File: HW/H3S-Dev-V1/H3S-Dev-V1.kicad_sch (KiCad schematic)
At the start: 50 parts, among them J1 USB_C_Receptacle_USB2.0_16P, J2 Conn_01x02, J3 Conn_Coaxial, J4 Conn_01x04, J5 Conn_01x04, Q1 DMP3099L, SW1 SW_Push, U1 Ra-01SH-P, U2 LTC4054ES5-4.2, U3 USBLC6-2SC6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

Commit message: Minor changes
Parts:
- C10, C11: footprint Capacitor_SMD:C_0603_1608Metric -> Capacitor_SMD:C_0402_1005Metric
- R18: footprint Resistor_SMD:R_0603_1608Metric -> Resistor_SMD:R_0402_1005Metric
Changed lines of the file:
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@@
 			)
 		)
-		(property "Footprint" "Resistor_SMD:R_0603_1608Metric"
+		(property "Footprint" "Resistor_SMD:R_0402_1005Metric"
 			(at 266.7 66.548 90)
 			(effects
@@
 			)
 		)
-		(property "Footprint" "Capacitor_SMD:C_0603_1608Metric"
+		(property "Footprint" "Capacitor_SMD:C_0402_1005Metric"
 			(at 272.7452 74.93 0)
 			(effects
@@
 			)
 		)
-		(property "Footprint" "Capacitor_SMD:C_0603_1608Metric"
+		(property "Footprint" "Capacitor_SMD:C_0402_1005Metric"
 			(at 262.5852 74.93 0)
 			(effects

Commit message: Some progress
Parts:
- added C12: 1u, Capacitor_SMD:C_0603_1608Metric, symbol Device:C
- added C13: 100n, Capacitor_SMD:C_0603_1608Metric, symbol Device:C
- added D2, D4: LED, LED_SMD:LED_0603_1608Metric, symbol Device:LED
- added R20, R21, R22: 10k, Resistor_SMD:R_0603_1608Metric, symbol Device:R
- added R23, R24, R25, R26, R27: 20, Resistor_SMD:R_0603_1608Metric, symbol Device:R
- added R28, R29: 0, Resistor_SMD:R_0603_1608Metric, symbol Device:R
- added SW2: SW_Push, Button_Switch_SMD:SW_Tactile_SPST_NO_Straight_CK_PTS636Sx25SMTRLFS, symbol Switch:SW_Push
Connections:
- net GND: now also C12.2, C13.2, R21.2, R22.2, SW2.2
- net SCL: now also R28.1
- net SDA: now also R29.1
- net VCC: now also D2.2 (A), R20.1
- net G_3D: now reaches U6.2 (3D_FIX)
- net G_JD: now reaches U6.20 (JAM_DET)
- net ~{G_RESET}: now reaches U6.23 (~{RESET})
- net ~{G_RESET}: now also R25.2
- net G_GF: now reaches U6.24 (GEO_FENCE)
- net G_TX: now reaches U6.25 (TXD1)
- net G_TX: now also R24.2
- net G_RX: now reaches U6.26 (RXD1)
- net G_RX: now also R23.2
- net G_FO: now reaches U6.28 (FORCE_ON)
- net G_FO: now also R27.2
- net G_TP: now reaches U6.29 (TIMEPULSE)
- net G_TP: now also D4.2 (A)
- net G_SDA: now reaches U6.3 (I2C_SDA)
- net G_SDA: now also R29.2
- net G_SCL: now reaches U6.6 (I2C_SCL)
- net G_SCL: now also R28.2
- net G_INT: now reaches U6.7 (EXTINT0)
- net G_INT: now also R26.2
- net ~{ESP_IO0}: now reaches U4.27 (IO0)
- net ~{ESP_IO0}: now also C12.1, C13.1, R20.2, SW2.1
- new net: D2.1 (K), R21.1
- new net: D4.1 (K), R22.1
- new net FO: R27.1
- new net INT: R26.1
- new net RX: R23.1
- new net TX: R24.1
- new net ~{G_RST}: R25.1
- no-connect marks 8 -> 7
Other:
- note added: "BOOT"
- note added: "RESET"
- moved on the sheet: C1, C10, C11, C2, C3, C4, C5, C6, C7, C8, C9, D1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

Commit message: Some progress
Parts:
- added R30, R31, R32, R33: 0, Resistor_SMD:R_0603_1608Metric, symbol Device:R
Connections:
- net G_3D: now also R31.1
- net G_GF: now also R32.1
- net G_JD: now also R33.1
- net G_TP: now also R30.1
- new net 3D: R31.2
- new net GF: R32.2
- new net JD: R33.2
- new net TP: R30.2
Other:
- moved on the sheet: C1, C10, C11, C12, C13, C2, C3, C4, C5, C6, C7, C8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

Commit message: Some progress
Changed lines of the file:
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@@
 	(wire
 		(pts
-			(xy 92.71 134.62) (xy 92.71 151.13)
+			(xy 92.71 134.62) (xy 92.71 152.4)
 		)
 		(stroke
@@
 	(symbol
 		(lib_id "power:GND")
-		(at 92.71 151.13 0)
+		(at 92.71 152.4 0)
 		(unit 1)
 		(exclude_from_sim no)
@@
 		(fields_autoplaced yes)
 		(property "Reference" "#PWR017"
-			(at 92.71 157.48 0)
+			(at 92.71 158.75 0)
 			(effects
 				(font
@@
 		)
 		(property "Value" "GND"
-			(at 92.71 156.21 0)
+			(at 92.71 157.48 0)
 			(effects
 				(font
@@
 		)
 		(property "Footprint" ""
-			(at 92.71 151.13 0)
+			(at 92.71 152.4 0)
 			(effects
 				(font
@@
 		)
 		(property "Datasheet" ""
-			(at 92.71 151.13 0)
+			(at 92.71 152.4 0)
 			(effects
 				(font
@@
 		)
 		(property "Description" "Power symbol creates a global label with name \"GND\" , ground"
-			(at 92.71 151.13 0)
+			(at 92.71 152.4 0)
 			(effects
 				(font

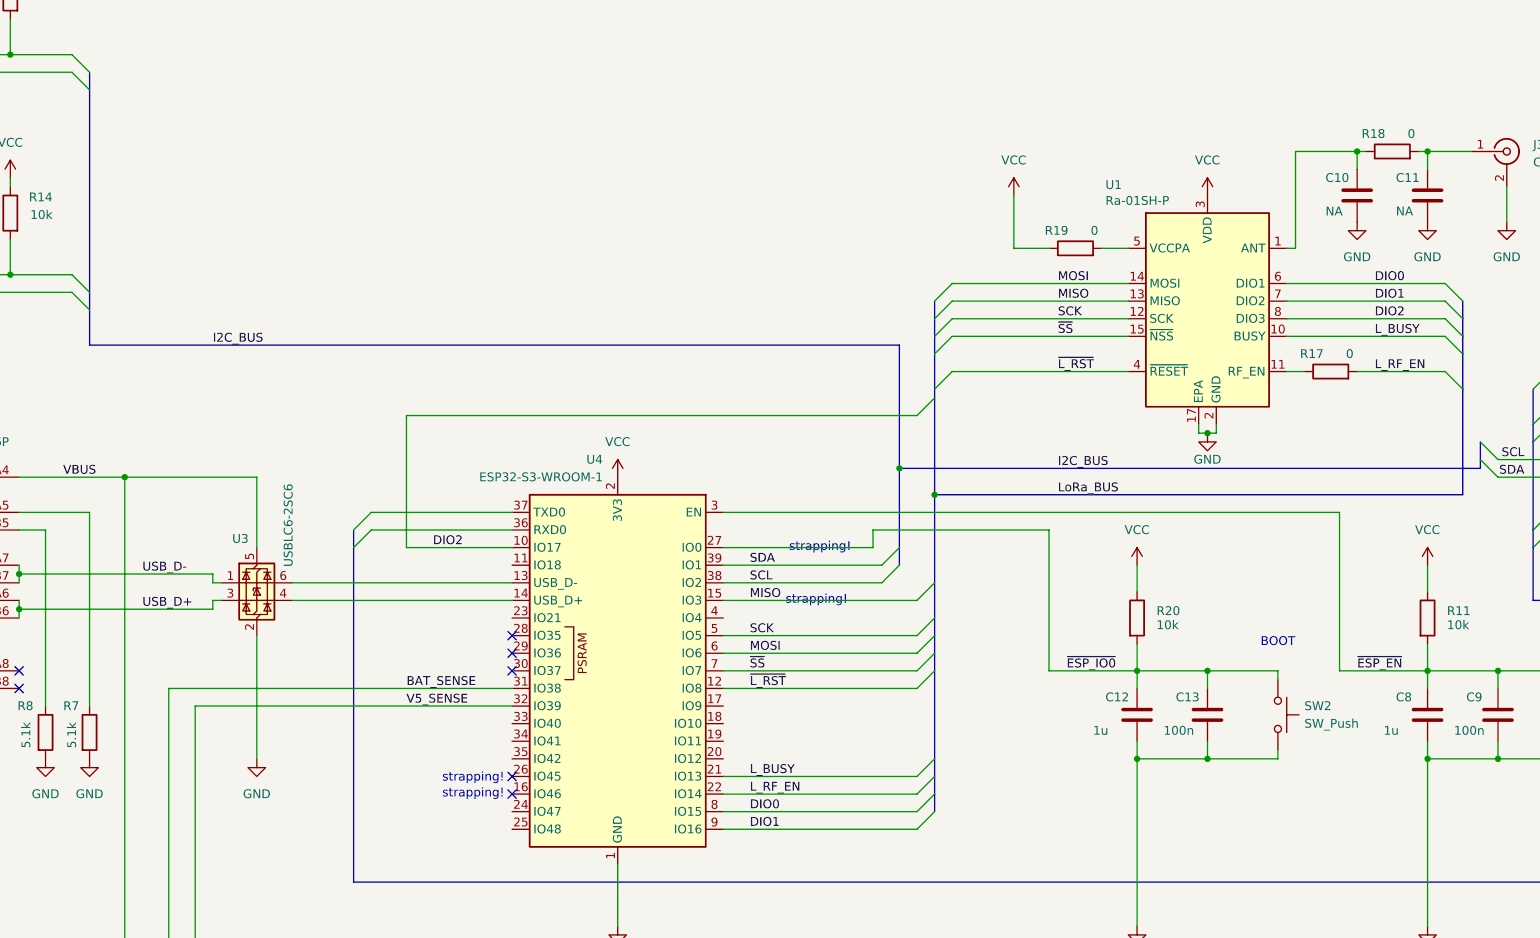
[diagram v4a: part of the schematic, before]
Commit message: LoRa intereface connected
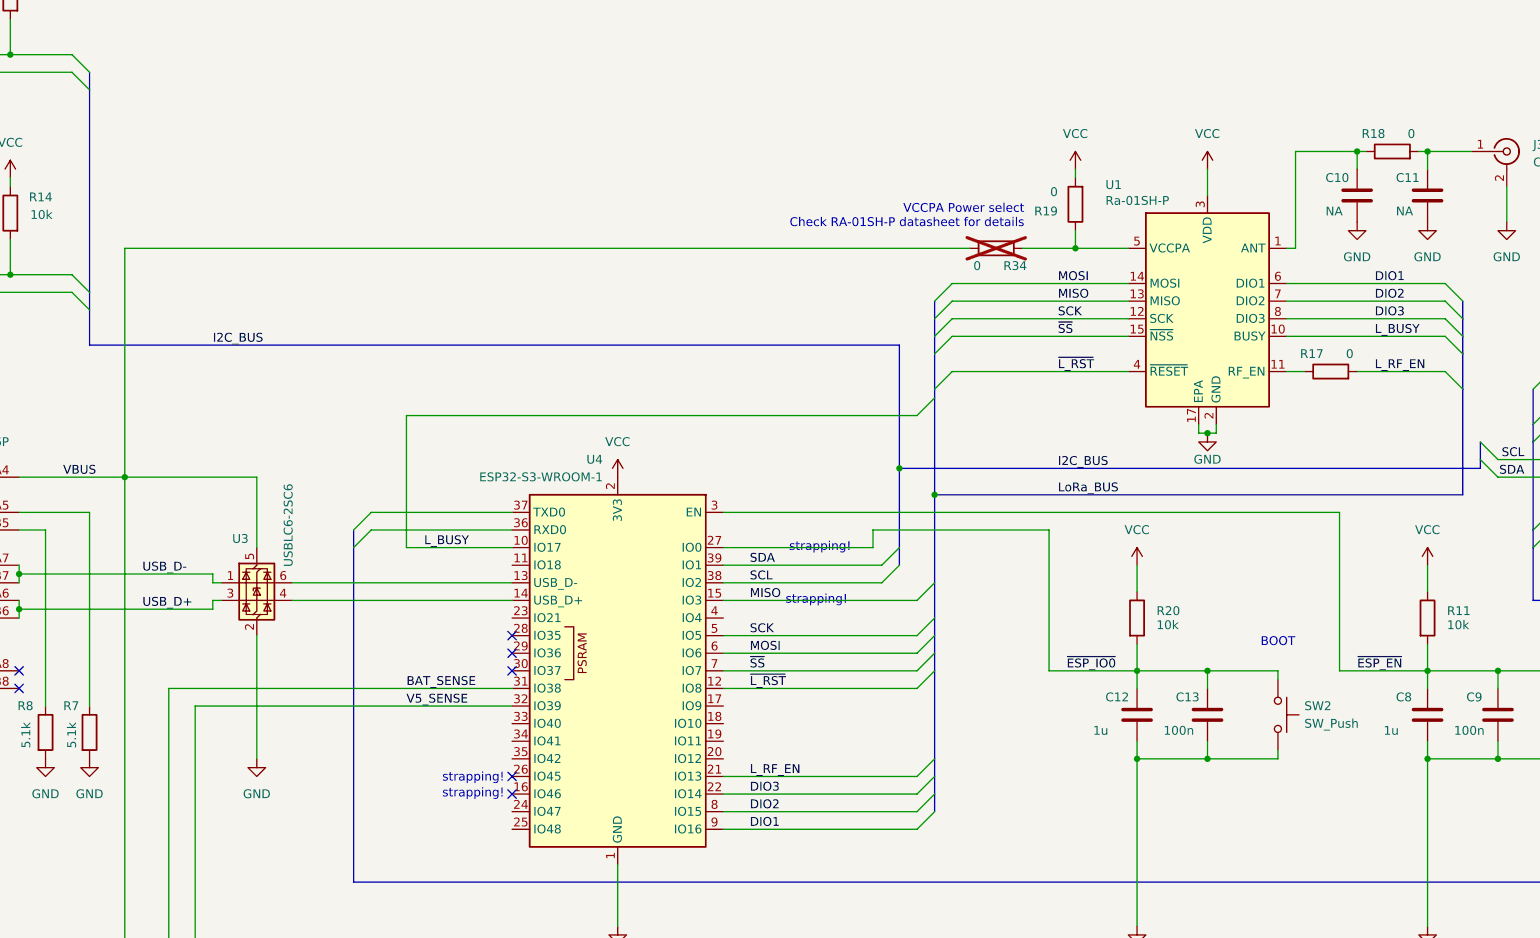
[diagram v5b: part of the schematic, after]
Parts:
- added R34: 0, Resistor_SMD:R_0603_1608Metric, symbol Device:R
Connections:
- net DIO1: now also U1.6 (DIO1); no longer U1.7 (DIO2)
- net DIO2: now also U1.7 (DIO2), U4.8 (IO15); no longer U1.8 (DIO3), U4.10 (IO17)
- net L_BUSY: now also U4.10 (IO17); no longer U4.21 (IO13)
- net L_RF_EN: now also U4.21 (IO13); no longer U4.22 (IO14)
- net VBUS: now also R34.2
- net VCC: now also R19.2; no longer R19.1
- net at U1.5 (VCCPA): now also R19.1, R34.1; no longer R19.2
- removed net DIO0: U1.6 (DIO1), U4.8 (IO15)
- new net DIO3: U1.8 (DIO3), U4.22 (IO14)
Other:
- note added: "VCCPA Power select Check RA-01SH-P datasheet for details"
- moved on the sheet: R19
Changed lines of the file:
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@@
 		)
 	)
+	(text "VCCPA Power select\nCheck RA-01SH-P datasheet for details"
+		(exclude_from_sim no)
+		(at 203.454 74.168 0)
+		(effects
+			(font
+				(size 1.27 1.27)
+			)
+			(justify right)
+		)
+	)
 	(text "strapping!"
 		(exclude_from_sim no)
@@
 	)
 	(junction
+		(at 210.82 78.74)
+		(diameter 0)
+		(color 0 0 0 0)
+	)
+	(junction
 		(at 360.68 88.9)
 		(diameter 0)
@@
 	(wire
 		(pts
+			(xy 210.82 78.74) (xy 218.44 78.74)
+		)
+		(stroke
+			(width 0)
+			(type default)
+		)
+	)
+	(wire
+		(pts
 			(xy 299.72 109.22) (xy 307.34 109.22)
 		)
@@
 	(wire
 		(pts
-			(xy 201.93 78.74) (xy 201.93 71.12)
-		)
-		(stroke
-			(width 0)
-			(type default)
-		)
-	)
-	(wire
-		(pts
 			(xy 240.03 152.4) (xy 240.03 151.13)
 		)
@@
 	(wire
 		(pts
+			(xy 203.2 78.74) (xy 210.82 78.74)
+		)
+		(stroke
+			(width 0)
+			(type default)
+		)
+	)
+	(wire
+		(pts
 			(xy 353.06 149.86) (xy 353.06 152.4)
 		)
@@
 	(wire
 		(pts
+			(xy 73.66 78.74) (xy 73.66 111.76)
+		)
+		(stroke
+			(width 0)
+			(type default)
+		)
+	)
+	(wire
+		(pts
 			(xy 92.71 111.76) (xy 73.66 111.76)
 		)
@@
 	(wire
 		(pts
-			(xy 214.63 78.74) (xy 218.44 78.74)
-		)
-		(stroke
-			(width 0)
-			(type default)
-		)
-	)
-	(wire
-		(pts
 			(xy 353.06 127) (xy 353.06 129.54)
 		)
@@
 	(wire
 		(pts
+			(xy 210.82 76.2) (xy 210.82 78.74)
+		)
+		(stroke
+			(width 0)
+			(type default)
+		)
+	)
+	(wire
+		(pts
 			(xy 261.62 64.77) (xy 261.62 67.31)
 		)
@@
 	(wire
 		(pts
+			(xy 210.82 68.58) (xy 210.82 67.31)
+		)
+		(stroke
+			(width 0)
+			(type default)
+		)
+	)
+	(wire
+		(pts
 			(xy 58.42 124.46) (xy 58.42 125.73)
 		)
@@
 	(wire
 		(pts
+			(xy 195.58 78.74) (xy 73.66 78.74)
+		)
+		(stroke
+			(width 0)
+			(type default)
+		)
+	)
+	(wire
+		(pts
 			(xy 58.42 116.84) (xy 68.58 116.84)
 		)
@@
 	(wire
 		(pts
-			(xy 207.01 78.74) (xy 201.93 78.74)
-		)
-		(stroke
-			(width 0)
-			(type default)
-		)
-	)
-	(wire
-		(pts
 			(xy 193.04 83.82) (xy 218.44 83.82)
 		)
@@
 	(wire
 		(pts
+			(xy 229.87 67.31) (xy 229.87 71.12)
+		)
+		(stroke
+			(width 0)
+			(type default)
+		)
+	)
+	(wire
+		(pts
 			(xy 386.08 116.84) (xy 393.7 116.84)
 		)
@@
 		)
 	)
+	(label "L_BUSY"
+		(at 116.84 121.92 0)
+		(effects
+			(font
+				(size 1.27 1.27)
+			)
+			(justify left bottom)
+		)
+	)
 	(label "SDA"
 		(at 275.59 111.76 180)
@@
 		)
 	)
+	(label "DIO3"
+		(at 163.83 157.48 0)
+		(effects
+			(font
+				(size 1.27 1.27)
+			)
+			(justify left bottom)
+		)
+	)
 	(label "G_BUS"
 		(at 284.48 170.18 0)
@@
 		)
 	)
-	(label "DIO0"
+	(label "DIO1"
 		(at 254 83.82 0)
 		(effects
@@
 		)
 	)
-	(label "DIO1"
+	(label "DIO2"
 		(at 254 86.36 0)
 		(effects
@@
 		)
 	)
-	(label "L_RF_EN"
-		(at 163.83 157.48 0)
-		(effects
-			(font
-				(size 1.27 1.27)
-			)
-			(justify left bottom)
-		)
-	)
 	(label "VBAT"
 		(at 44.45 196.85 0)
@@
 		)
 	)
-	(label "DIO2"
+	(label "DIO3"
 		(at 254 88.9 0)
 		(effects
@@
 		)
 	)
-	(label "L_BUSY"
-		(at 163.83 154.94 0)
-		(effects
-			(font
-				(size 1.27 1.27)
-			)
-			(justify left bottom)
-		)
-	)
 	(label "DIO1"
 		(at 163.83 162.56 0)
@@
 		)
 	)
+	(label "L_RF_EN"
+		(at 163.83 154.94 0)
+		(effects
+			(font
+				(size 1.27 1.27)
+			)
+			(justify left bottom)
+		)
+	)
 	(label "JD"
 		(at 388.62 116.84 0)
@@
 		)
 	)
-	(label "DIO2"
-		(at 118.11 121.92 0)
-		(effects
-			(font
-				(size 1.27 1.27)
-			)
-			(justify left bottom)
-		)
-	)
 	(label "TX"
 		(at 279.4 104.14 0)
@@
 		)
 	)
-	(label "DIO0"
+	(label "DIO2"
 		(at 163.83 160.02 0)
 		(effects
@@
 	)
 	(symbol
+		(lib_id "Device:R")
+		(at 199.39 78.74 270)
+		(unit 1)
+		(exclude_from_sim no)
+		(in_bom yes)
+		(on_board yes)
+		(dnp yes)
+		(property "Reference" "R34"
+			(at 200.406 81.28 90)
+			(effects
+				(font
+					(size 1.27 1.27)
+				)
+				(justify left)
+			)
+		)
+		(property "Value" "0"
+			(at 196.088 81.28 90)
+			(effects
+				(font
+					(size 1.27 1.27)
+				)
+				(justify left)
+			)
+		)
+		(property "Footprint" "Resistor_SMD:R_0603_1608Metric"
+			(at 199.39 76.962 90)
+			(effects
+				(font
+					(size 1.27 1.27)
+				)
+				(hide yes)
+			)
+		)
+		(property "Datasheet" "~"
+			(at 199.39 78.74 0)
+			(effects
+				(font
+					(size 1.27 1.27)
+				)
+				(hide yes)
+			)
+		)
+		(property "Description" "Resistor"
+			(at 199.39 78.74 0)
+			(effects
+				(font
+					(size 1.27 1.27)
+				)
+				(hide yes)
+			)
+		)
+		(pin "2"
+		)
+		(pin "1"
+		)
+		(instances
+			(project "H3S-Dev-V1"
+				(path "/bea38324-05bc-47f3-9040-a69798280d79"
+					(reference "R34")
+					(unit 1)
+				)
+			)
+		)
+	)
+	(symbol
 		(lib_id "Switch:SW_Push")
 		(at 240.03 146.05 270)
@@
 	(symbol
 		(lib_id "power:VCC")
-		(at 201.93 71.12 0)
+		(at 210.82 67.31 0)
 		(unit 1)
 		(exclude_from_sim no)
@@
 		(fields_autoplaced yes)
 		(property "Reference" "#PWR040"
-			(at 201.93 74.93 0)
+			(at 210.82 71.12 0)
 			(effects
 				(font
@@
 		)
 		(property "Value" "VCC"
-			(at 201.93 66.04 0)
+			(at 210.82 62.23 0)
 			(effects
 				(font
@@
 		)
 		(property "Footprint" ""
-			(at 201.93 71.12 0)
+			(at 210.82 67.31 0)
 			(effects
 				(font
@@
 		)
 		(property "Datasheet" ""
-			(at 201.93 71.12 0)
+			(at 210.82 67.31 0)
 			(effects
 				(font
@@
 		)
 		(property "Description" "Power symbol creates a global label with name \"VCC\""
-			(at 201.93 71.12 0)
+			(at 210.82 67.31 0)
 			(effects
 				(font
@@
 	(symbol
 		(lib_id "Device:R")
-		(at 210.82 78.74 90)
+		(at 210.82 72.39 180)
 		(unit 1)
 		(exclude_from_sim no)
@@
 		(dnp no)
 		(property "Reference" "R19"
-			(at 209.804 76.2 90)
+			(at 208.28 73.406 0)
 			(effects
 				(font
@@
 		)
 		(property "Value" "0"
-			(at 214.122 76.2 90)
+			(at 208.28 70.612 0)
 			(effects
 				(font
@@
 		)
 		(property "Footprint" "Resistor_SMD:R_0603_1608Metric"
-			(at 210.82 80.518 90)
+			(at 212.598 72.39 90)
 			(effects
 				(font
@@
 		)
 		(property "Datasheet" "~"
-			(at 210.82 78.74 0)
+			(at 210.82 72.39 0)
 			(effects
 				(font
@@
 		)
 		(property "Description" "Resistor"
-			(at 210.82 78.74 0)
+			(at 210.82 72.39 0)
 			(effects
 				(font
@@
 	(symbol
 		(lib_id "power:VCC")
-		(at 229.87 71.12 0)
+		(at 229.87 67.31 0)
 		(unit 1)
 		(exclude_from_sim no)
@@
 		(fields_autoplaced yes)
 		(property "Reference" "#PWR013"
-			(at 229.87 74.93 0)
+			(at 229.87 71.12 0)
 			(effects
 				(font
@@
 		)
 		(property "Value" "VCC"
-			(at 229.87 66.04 0)
+			(at 229.87 62.23 0)
 			(effects
 				(font
@@
 		)
 		(property "Footprint" ""
-			(at 229.87 71.12 0)
+			(at 229.87 67.31 0)
 			(effects
 				(font
@@
 		)
 		(property "Datasheet" ""
-			(at 229.87 71.12 0)
+			(at 229.87 67.31 0)
 			(effects
 				(font
@@
 		)
 		(property "Description" "Power symbol creates a global label with name \"VCC\""
-			(at 229.87 71.12 0)
+			(at 229.87 67.31 0)
 			(effects
 				(font
